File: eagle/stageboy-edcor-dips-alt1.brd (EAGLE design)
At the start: 120 x 75 mm, 38 parts, among them IC1 MEGA8-P, IC2 7805TV, J1 POWER_JACKPTH, Q1 16MHz, X1 MIDI IN, X2 MIDI OUT, X4 22-23-2021, X6 GBIO

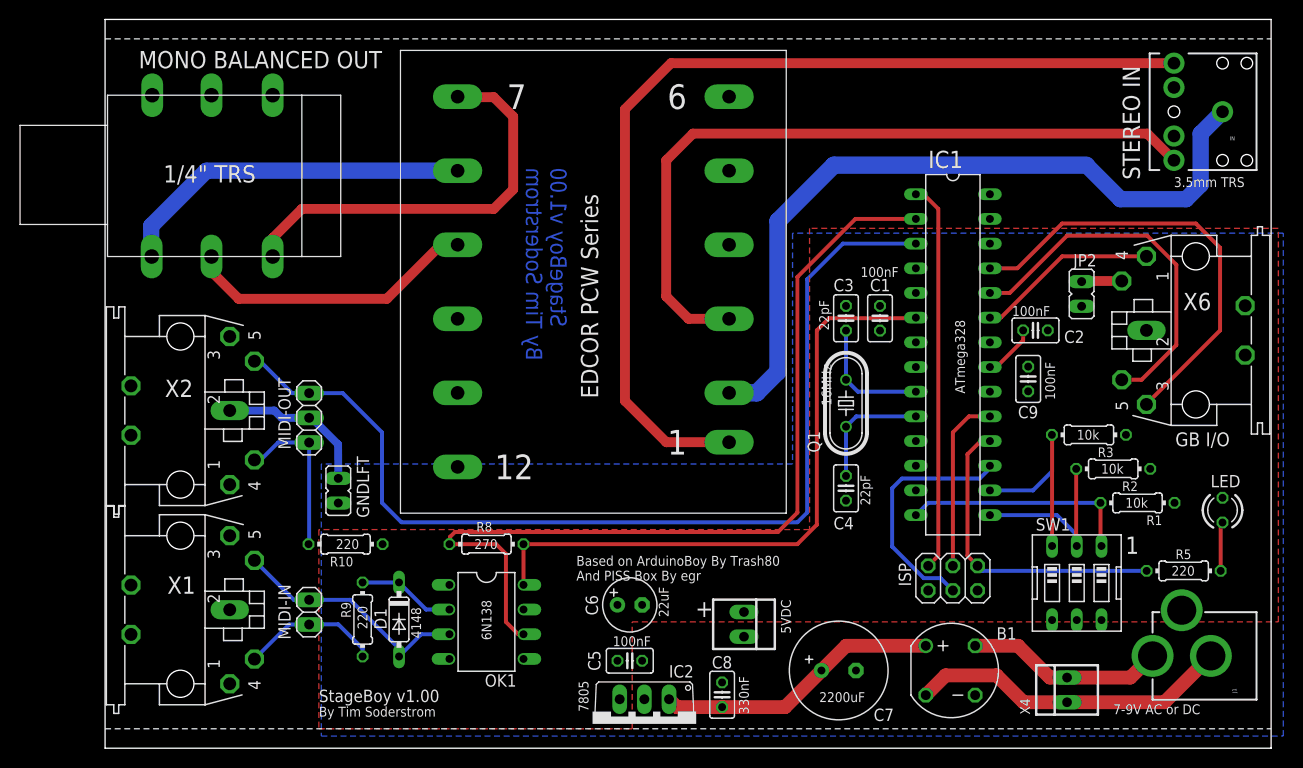
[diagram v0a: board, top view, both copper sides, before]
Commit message: Added an alternate board layout
This layout moves the AVR down further away from the analog
bits and expands the ground and power planes, while also
replacing the pull-down resistors with the internal AVR
pull-ups.
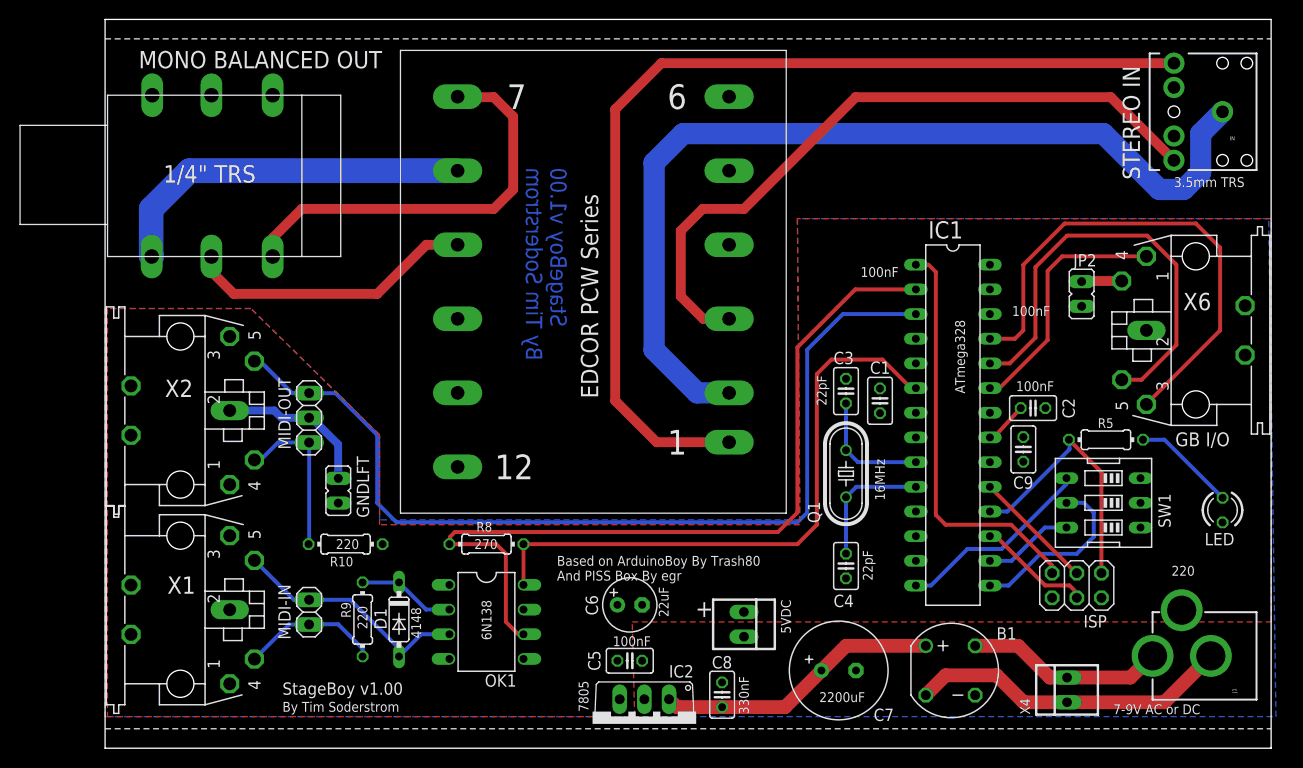
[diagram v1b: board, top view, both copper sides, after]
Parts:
- removed R1, R2, R3: 10k, resistor:0204/7
- moved R5 15.7 mm to (103.0, 31.8)
- moved ISP 12.8 mm to (100.0, 16.8)
- moved SW1 8.70 mm to (102.8, 25.2), turned to 90 degrees
- moved C1 8.50 mm to (79.8, 35.8)
- moved C2 8.00 mm to (95.5, 35.0)
- moved C4 8.00 mm to (76.2, 18.8)
- moved C3 7.50 mm to (76.2, 36.8)
- moved C9 7.27 mm to (94.5, 30.8)
- moved IC1 7.25 mm to (87.2, 33.2)
- moved Q1 7.25 mm to (76.2, 28.2)
- turned LED to 270 degrees
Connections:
- removed net N$14: IC1.15, R2.2, SW1.2
- removed net N$15: IC1.16, R3.2, SW1.3
- new net N$5: IC1.15, SW1.5
- new net N$6: IC1.16, SW1.6
- net +5V: no longer SW1.4, SW1.5, SW1.6
- net GND: now also SW1.1, SW1.2, SW1.3; no longer R1.1, R2.1, R3.1
- net N$4: now also SW1.4; no longer R1.2, SW1.1
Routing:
- net N$15: track 22.4 -> 0.00 mm
- net N$14: track 18.9 -> 0.00 mm
- net N$35: track 77.8 -> 96.6 mm
- net N$5: track 0.00 -> 18.5 mm
- net N$17: track 25.3 -> 11.9 mm
- net N$6: track 0.00 -> 9.30 mm
- net N$21: track 105.1 -> 97.7 mm
- net N$25: track 38.2 -> 45.5 mm
- net N$11: track 92.0 -> 84.8 mm
- net N$26: track 18.7 -> 25.9 mm
- net N$23: track 46.0 -> 52.9 mm
- net N$3: track 5.06 -> 10.7 mm
- net N$19: track 18.2 -> 12.6 mm
- net N$18: track 32.4 -> 27.0 mm
- net N$40: track 76.0 -> 71.8 mm
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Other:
- board text removed: "1"
- board text removed: "10k"

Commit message: Routing optimizations
Made some routing optimizations in the analog section.
Bigger traces and more direct routing.
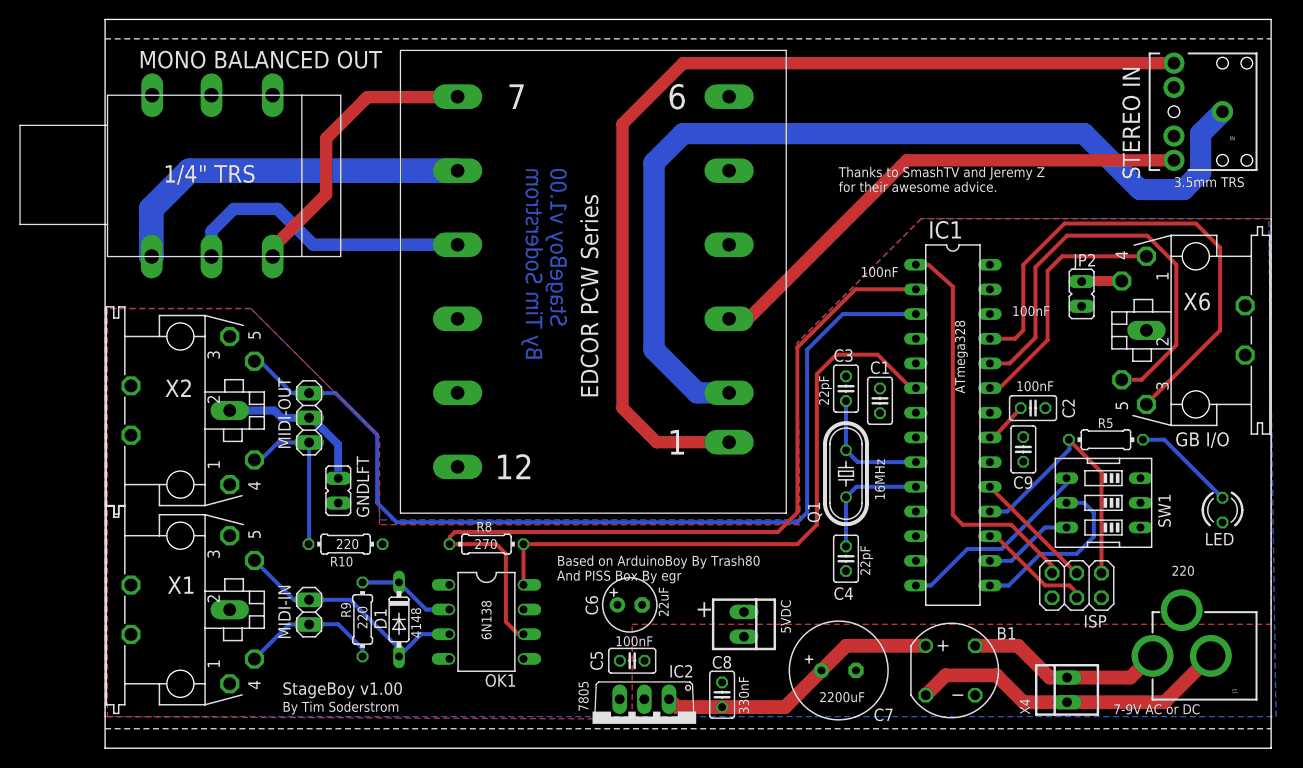
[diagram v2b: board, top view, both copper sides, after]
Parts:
- moved C4 0.75 mm to (76.2, 19.5)
- moved C3 0.25 mm to (76.2, 37.0)
- moved C5 0.25 mm to (54.2, 9.00)
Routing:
- net N$40: track 71.8 -> 52.5 mm
- net N$32: track 42.8 -> 29.7 mm
- net N$29: track 103.0 -> 101.0 mm
- net N$1: track 42.3 -> 41.3 mm
- net N$22: track 13.4 -> 12.7 mm
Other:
- board text added: "Thanks to SmashTV and Jeremy Z for their awesome advice."

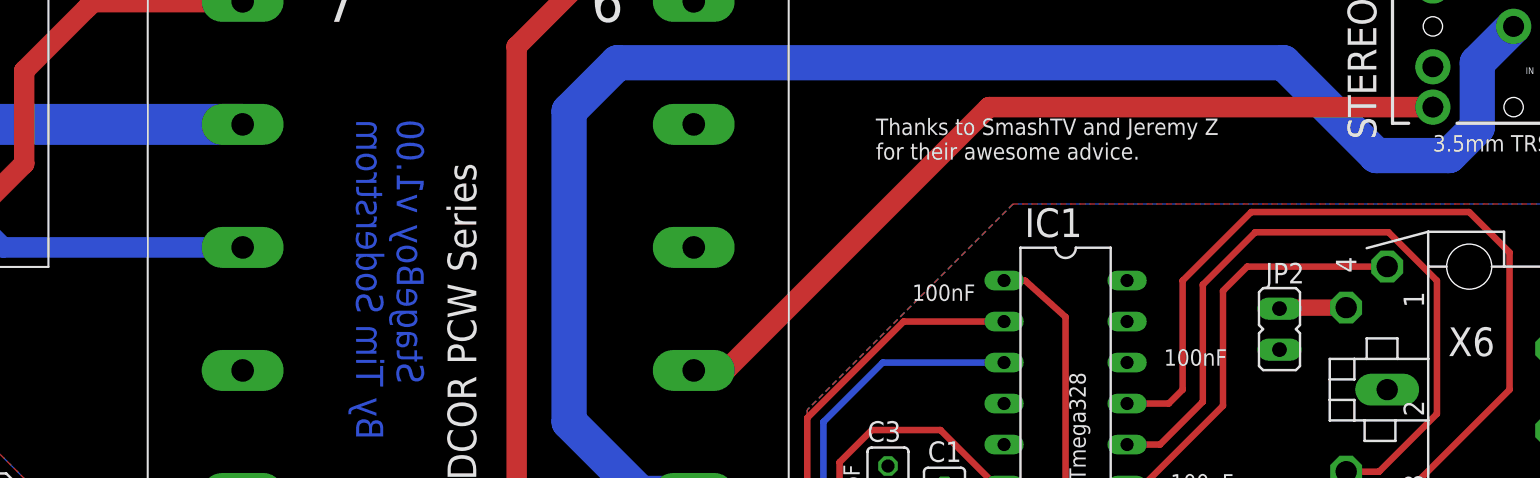
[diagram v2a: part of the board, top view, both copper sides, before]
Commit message: Added holes for zip-ties
Added holes to run zipties through for the tranny.
Thought I already added these?
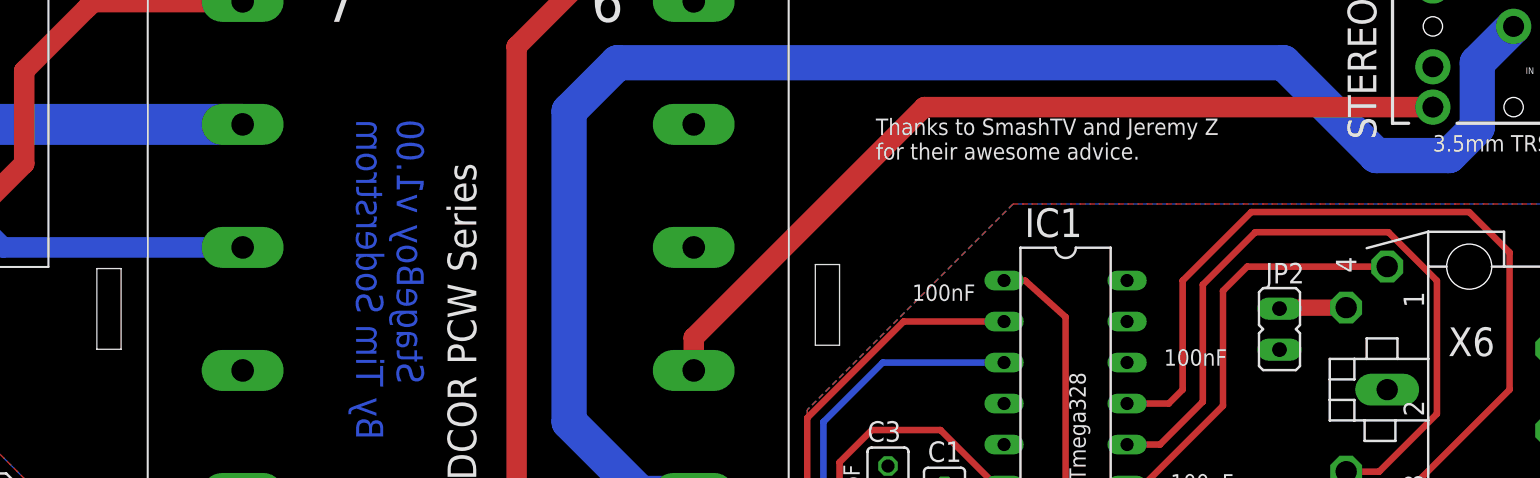
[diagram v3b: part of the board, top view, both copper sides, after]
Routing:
- net N$40: track 52.5 -> 53.7 mm
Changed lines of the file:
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@@
 <text x="75.5" y="57.25" size="1.016" layer="25">Thanks to SmashTV and Jeremy Z
 for their awesome advice.</text>
+<wire x1="27.25" y1="50.5" x2="27.25" y2="45.5" width="0" layer="21"/>
+<wire x1="27.25" y1="45.5" x2="28.75" y2="45.5" width="0" layer="21"/>
+<wire x1="28.75" y1="45.5" x2="28.75" y2="50.5" width="0" layer="21"/>
+<wire x1="28.75" y1="50.5" x2="27.25" y2="50.5" width="0" layer="21"/>
+<wire x1="71.75" y1="50.75" x2="71.75" y2="45.75" width="0" layer="21"/>
+<wire x1="71.75" y1="45.75" x2="73.25" y2="45.75" width="0" layer="21"/>
+<wire x1="73.25" y1="45.75" x2="73.25" y2="50.75" width="0" layer="21"/>
+<wire x1="73.25" y1="50.75" x2="71.75" y2="50.75" width="0" layer="21"/>
 </plain>
 <attributes>
@@
 <contactref element="IN" pad="RING"/>
 <contactref element="U$1" pad="P$3"/>
-<wire x1="110" y1="60.5" x2="82.5" y2="60.5" width="1.27" layer="1"/>
-<wire x1="82.5" y1="60.5" x2="66.25" y2="44.25" width="1.27" layer="1"/>
-<wire x1="66.25" y1="44.25" x2="64.28" y2="44.25" width="1.27" layer="1"/>
-<wire x1="64.28" y1="44.25" x2="64.22" y2="44.19" width="1.27" layer="1"/>
+<wire x1="110" y1="60.5" x2="78.5" y2="60.5" width="1.27" layer="1"/>
+<wire x1="66.25" y1="44.25" x2="64.28" y2="44.25" width="0" layer="19" extent="1-16"/>
+<wire x1="64.28" y1="44.25" x2="64.22" y2="44.19" width="0" layer="19" extent="1-16"/>
+<wire x1="78.5" y1="60.5" x2="64.22" y2="46.22" width="1.27" layer="1"/>
+<wire x1="64.22" y1="44.19" x2="64.22" y2="46.22" width="1.27" layer="1"/>
 </signal>
 <signal name="N$3">
